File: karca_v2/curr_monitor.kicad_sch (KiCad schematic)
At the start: 25 parts, among them U30 INA180A4, U32 NUP4202

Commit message: fkkkkkkkkkk
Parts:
- U32: footprint Package_SO:TSOP-6_1.65x3.05mm_P0.95mm -> Package_TO_SOT_SMD:SOT-363_SC-70-6
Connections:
- net DRV1_ADC: now also U32.4; no longer U32.1
- net DRV2_ADC: now also U32.3; no longer U32.6
- net DRV3_ADC: now also U32.1; no longer U32.4
- net DRV4_ADC: now also U32.6; no longer U32.3
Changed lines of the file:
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@@
   (junction (at 173.99 52.07) (diameter 0) (color 0 0 0 0)
   )
-  (junction (at 213.36 129.54) (diameter 0) (color 0 0 0 0)
-  )
   (junction (at 158.75 52.07) (diameter 0) (color 0 0 0 0)
   )
-  (junction (at 208.28 77.47) (diameter 0) (color 0 0 0 0)
+  (junction (at 208.28 106.68) (diameter 0) (color 0 0 0 0)
   )
   (junction (at 101.6 147.32) (diameter 0) (color 0 0 0 0)
@@
   (junction (at 173.99 153.67) (diameter 0) (color 0 0 0 0)
   )
-  (junction (at 217.17 92.71) (diameter 0) (color 0 0 0 0)
-  )
-  (junction (at 238.76 83.185) (diameter 0) (color 0 0 0 0)
-  )
   (junction (at 101.6 123.19) (diameter 0) (color 0 0 0 0)
   )
@@
   (junction (at 222.25 153.67) (diameter 0) (color 0 0 0 0)
   )
+  (junction (at 201.295 77.47) (diameter 0) (color 0 0 0 0)
+  )
+  (junction (at 198.12 129.54) (diameter 0) (color 0 0 0 0)
+  )
   (junction (at 173.99 83.82) (diameter 0) (color 0 0 0 0)
   )
@@
   (junction (at 158.75 106.68) (diameter 0) (color 0 0 0 0)
   )
+  (junction (at 213.36 52.07) (diameter 0) (color 0 0 0 0)
+  )
   (junction (at 173.99 106.68) (diameter 0) (color 0 0 0 0)
   )
@@
     (stroke (width 0) (type default))
   )
-  (wire (pts (xy 238.76 83.185) (xy 238.76 52.07))
+  (wire (pts (xy 238.76 52.07) (xy 238.76 87.63))
     (stroke (width 0) (type default))
   )
@@
     (stroke (width 0) (type default))
   )
+  (wire (pts (xy 208.28 99.06) (xy 208.28 106.68))
+    (stroke (width 0) (type default))
+  )
   (wire (pts (xy 107.95 86.36) (xy 104.14 86.36))
     (stroke (width 0) (type default))
@@
     (stroke (width 0) (type default))
   )
-  (wire (pts (xy 173.99 52.07) (xy 238.76 52.07))
+  (wire (pts (xy 173.99 52.07) (xy 213.36 52.07))
     (stroke (width 0) (type default))
   )
@@
     (stroke (width 0) (type default))
   )
+  (wire (pts (xy 213.36 52.07) (xy 238.76 52.07))
+    (stroke (width 0) (type default))
+  )
   (wire (pts (xy 107.95 132.08) (xy 107.95 135.89))
     (stroke (width 0) (type default))
@@
     (stroke (width 0) (type default))
   )
+  (wire (pts (xy 208.28 106.68) (xy 217.17 106.68))
+    (stroke (width 0) (type default))
+  )
   (wire (pts (xy 158.75 158.75) (xy 158.75 153.67))
     (stroke (width 0) (type default))
@@
     (stroke (width 0) (type default))
   )
-  (wire (pts (xy 219.71 129.54) (xy 213.36 129.54))
-    (stroke (width 0) (type default))
-  )
   (wire (pts (xy 158.75 52.07) (xy 173.99 52.07))
     (stroke (width 0) (type default))
@@
     (stroke (width 0) (type default))
   )
-  (wire (pts (xy 213.36 87.63) (xy 213.36 88.9))
+  (wire (pts (xy 213.36 104.775) (xy 201.295 104.775))
     (stroke (width 0) (type default))
   )
@@
     (stroke (width 0) (type default))
   )
+  (wire (pts (xy 198.12 129.54) (xy 219.71 129.54))
+    (stroke (width 0) (type default))
+  )
+  (wire (pts (xy 201.295 104.775) (xy 201.295 77.47))
+    (stroke (width 0) (type default))
+  )
   (wire (pts (xy 101.6 54.61) (xy 93.98 54.61))
     (stroke (width 0) (type default))
@@
     (stroke (width 0) (type default))
   )
-  (wire (pts (xy 173.99 106.68) (xy 217.17 106.68))
+  (wire (pts (xy 173.99 106.68) (xy 208.28 106.68))
     (stroke (width 0) (type default))
   )
@@
     (stroke (width 0) (type default))
   )
-  (wire (pts (xy 203.835 99.06) (xy 208.28 99.06))
-    (stroke (width 0) (type default))
-  )
   (wire (pts (xy 229.235 90.17) (xy 238.76 90.17))
     (stroke (width 0) (type default))
   )
+  (wire (pts (xy 213.36 52.07) (xy 213.36 88.9))
+    (stroke (width 0) (type default))
+  )
   (wire (pts (xy 101.6 123.19) (xy 101.6 125.73))
     (stroke (width 0) (type default))
@@
     (stroke (width 0) (type default))
   )
-  (wire (pts (xy 217.17 92.71) (xy 217.17 87.63))
-    (stroke (width 0) (type default))
-  )
-  (wire (pts (xy 238.76 87.63) (xy 238.76 83.185))
-    (stroke (width 0) (type default))
-  )
   (wire (pts (xy 217.17 92.71) (xy 238.76 92.71))
     (stroke (width 0) (type default))
@@
     (stroke (width 0) (type default))
   )
+  (wire (pts (xy 201.295 77.47) (xy 229.235 77.47))
+    (stroke (width 0) (type default))
+  )
   (wire (pts (xy 107.95 77.47) (xy 107.95 81.28))
     (stroke (width 0) (type default))
@@
     (stroke (width 0) (type default))
   )
+  (wire (pts (xy 198.12 88.9) (xy 198.12 129.54))
+    (stroke (width 0) (type default))
+  )
   (wire (pts (xy 158.75 106.68) (xy 173.99 106.68))
     (stroke (width 0) (type default))
   )
+  (wire (pts (xy 208.28 88.9) (xy 198.12 88.9))
+    (stroke (width 0) (type default))
+  )
   (wire (pts (xy 93.98 54.61) (xy 93.98 55.88))
     (stroke (width 0) (type default))
@@
     (stroke (width 0) (type default))
   )
-  (wire (pts (xy 217.17 87.63) (xy 213.36 87.63))
-    (stroke (width 0) (type default))
-  )
   (wire (pts (xy 173.99 81.28) (xy 173.99 83.82))
     (stroke (width 0) (type default))
@@
     (stroke (width 0) (type default))
   )
+  (wire (pts (xy 213.36 99.06) (xy 213.36 104.775))
+    (stroke (width 0) (type default))
+  )
   (wire (pts (xy 158.75 88.9) (xy 158.75 83.82))
     (stroke (width 0) (type default))
@@
     (stroke (width 0) (type default))
   )
-  (wire (pts (xy 203.835 83.185) (xy 203.835 99.06))
-    (stroke (width 0) (type default))
-  )
   (wire (pts (xy 99.06 77.47) (xy 107.95 77.47))
     (stroke (width 0) (type default))
@@
     (stroke (width 0) (type default))
   )
-  (wire (pts (xy 208.28 77.47) (xy 229.235 77.47))
+  (wire (pts (xy 175.26 77.47) (xy 201.295 77.47))
     (stroke (width 0) (type default))
   )
@@
     (stroke (width 0) (type default))
   )
-  (wire (pts (xy 173.99 129.54) (xy 213.36 129.54))
-    (stroke (width 0) (type default))
-  )
-  (wire (pts (xy 175.26 77.47) (xy 208.28 77.47))
+  (wire (pts (xy 173.99 129.54) (xy 198.12 129.54))
     (stroke (width 0) (type default))
   )
@@
     (stroke (width 0) (type default))
   )
-  (wire (pts (xy 238.76 83.185) (xy 203.835 83.185))
-    (stroke (width 0) (type default))
-  )
-  (wire (pts (xy 213.36 99.06) (xy 213.36 129.54))
-    (stroke (width 0) (type default))
-  )
   (wire (pts (xy 121.92 106.68) (xy 146.05 106.68))
     (stroke (width 0) (type default))
@@
   )
   (wire (pts (xy 104.14 86.36) (xy 104.14 87.63))
-    (stroke (width 0) (type default))
-  )
-  (wire (pts (xy 208.28 77.47) (xy 208.28 88.9))
     (stroke (width 0) (type default))
   )
@@
       (effects (font (size 1.27 1.27)) (justify left))
     )
-    (property "Footprint" "Package_SO:TSOP-6_1.65x3.05mm_P0.95mm" (at 212.09 92.075 0)
-      (effects (font (size 1.27 1.27)) hide)
-    )
+    (property "Footprint" "Package_TO_SOT_SMD:SOT-363_SC-70-6" (at 212.09 92.075 0)
+      (effects (font (size 1.27 1.27)) hide)
+    )

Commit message: discrete traces
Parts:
- renumbered C51 to C66, C52 to C67, C54 to C68, C55 to C69, C56 to C70, C57 to C71, C58 to C72, R98 to R102, R99 to R103, R100 to R104, R101 to R105, R102 to R106, R103 to R107, R104 to R108, R105 to R109, R106 to R110, R107 to R111, U30 to U40, U31 to U41, U32 to U42

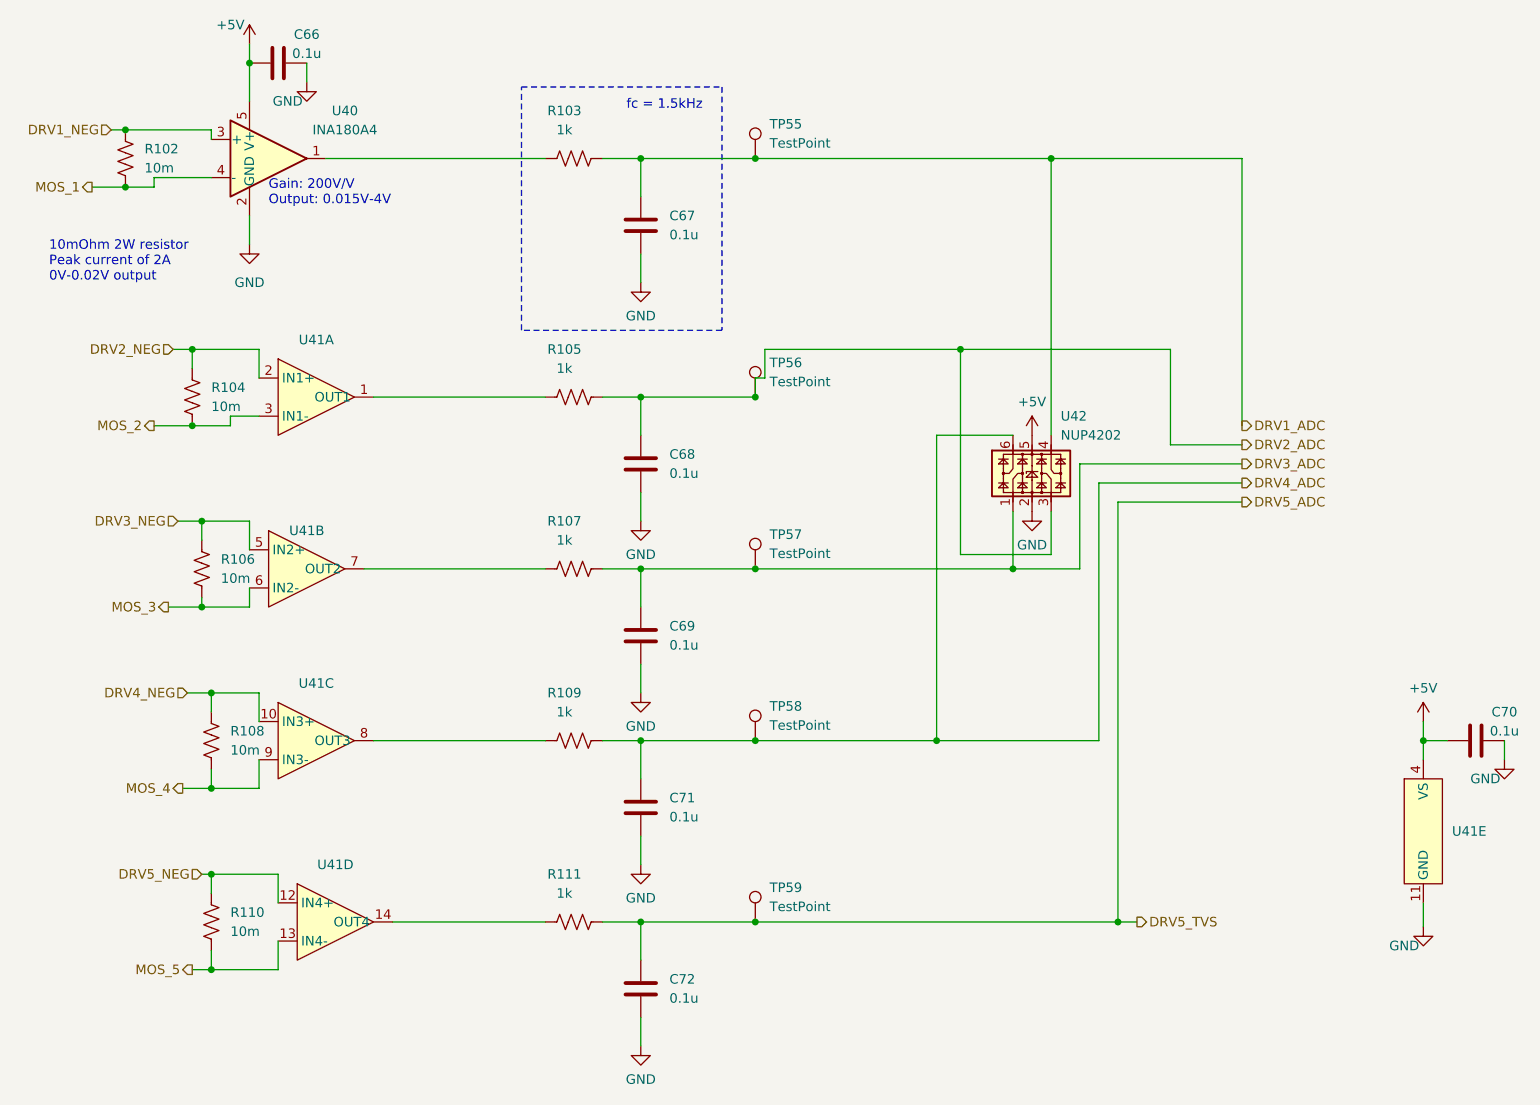
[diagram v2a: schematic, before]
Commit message: fixed TVS Diodes
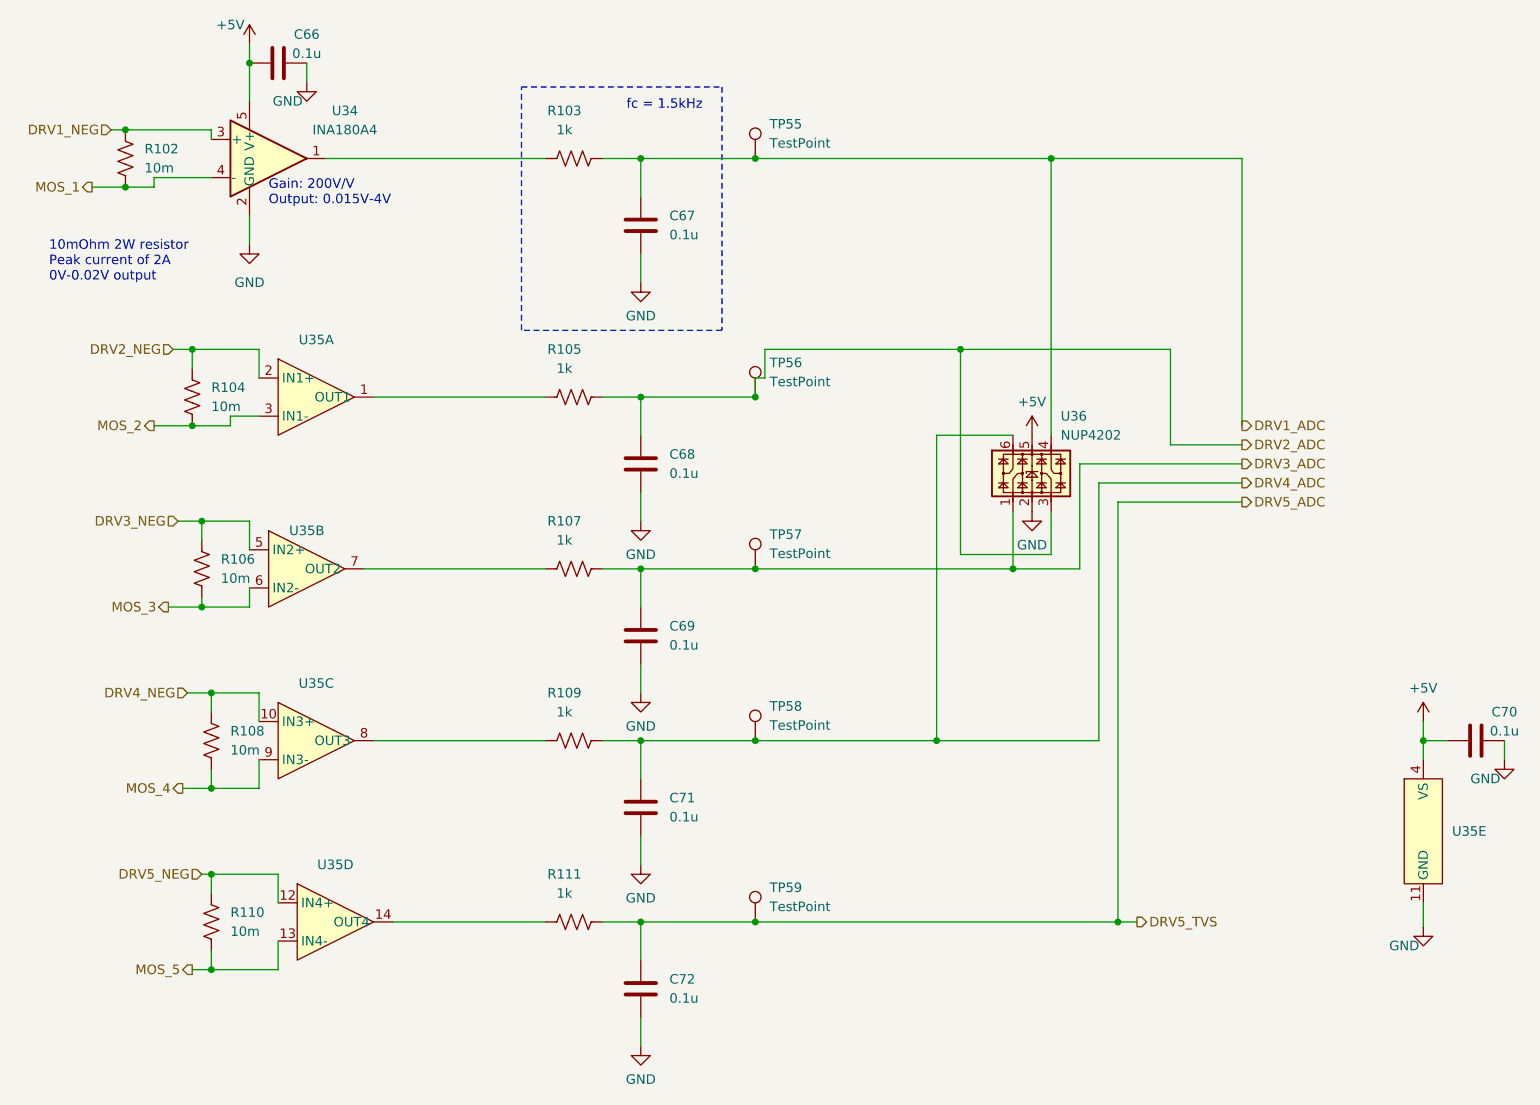
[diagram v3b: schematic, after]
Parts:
- renumbered U40 to U34, U41 to U35, U42 to U36

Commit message: Fixed ground capacitors
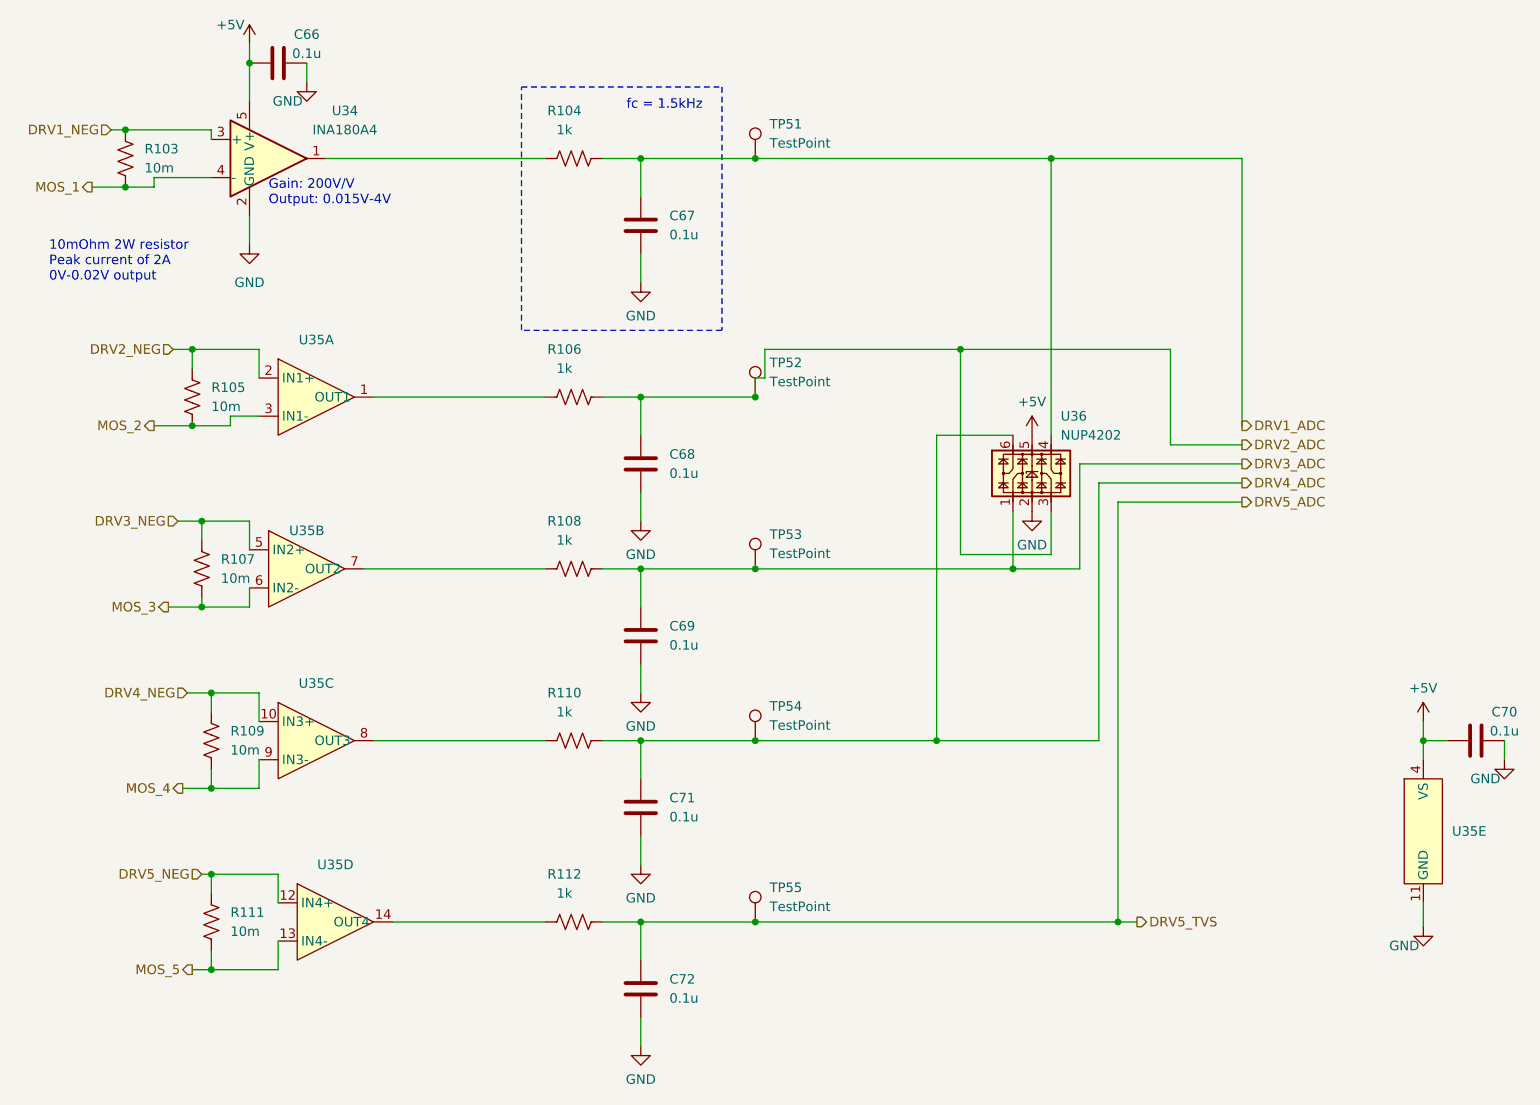
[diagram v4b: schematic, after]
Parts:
- renumbered R102 to R103, R103 to R104, R104 to R105, R105 to R106, R106 to R107, R107 to R108, R108 to R109, R109 to R110, R110 to R111, R111 to R112, TP55 to TP51, TP56 to TP52, TP57 to TP53, TP58 to TP54, TP59 to TP55

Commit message: Passed all DRC, Added safety jumper to isolate regulators from rest of the board
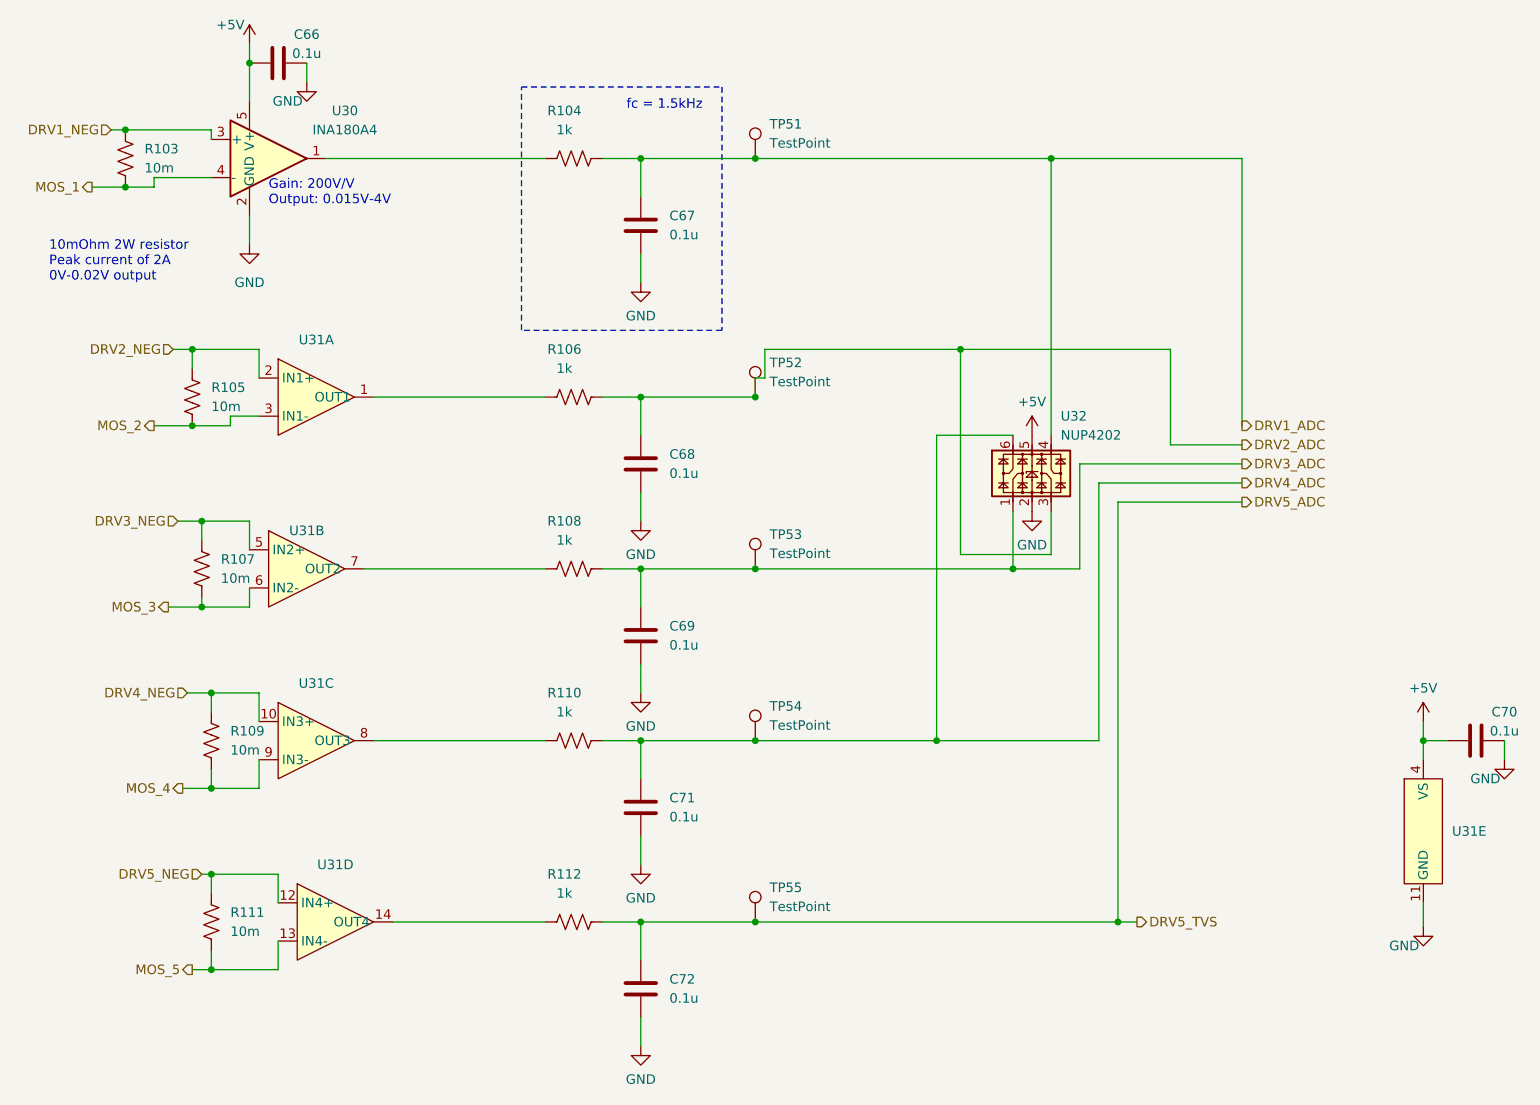
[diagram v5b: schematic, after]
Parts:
- renumbered U34 to U30, U35 to U31, U36 to U32
